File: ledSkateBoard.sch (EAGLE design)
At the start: 24 parts, among them U1 MPU-9150, U2 ATMEGA328P_TQFP, U4 MIC2505 3.3

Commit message: Initial route of board
Still need to add test pads for debugging.
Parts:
- removed D4, D5: (no value), SparkFun-DiscreteSemi:DIODESOD523
- added D2, D3: RB751, SparkFun-DiscreteSemi:DIODE-SCHOTTKY-RB751
- added JP3: LED CONNECTOR, SparkFun-Connectors:M03PTH
- added R6: 4.3K, SparkFun-Resistors:RESISTOR0603-RES
- added R7: 36K, SparkFun-Resistors:RESISTOR0603-RES
- added TP1: TEST-POINT3, SparkFun-Passives:TEST-POINT3
- J1: value (none) -> JST
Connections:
- new net DATA: JP3.2, U2.PB0(ICP)
- new net N$4: R6.1, R7.2, U2.PC0(ADC0)
- net 5V: now also D2.A; no longer D4.A
- net GND: now also JP3.3, R7.1
- net N$3: now also D2.C, D3.C; no longer D4.C, D5.C
- net VCC: now also U2.AREF
- net V_BATT: now also D3.A, JP3.1, R6.2; no longer D5.A
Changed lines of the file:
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@@
 <part name="C5" library="SparkFun-Capacitors" deviceset="CAP" device="PTH" value="4.7uF"/>
 <part name="GND10" library="SparkFun-Aesthetics" deviceset="GND" device=""/>
-<part name="J1" library="SparkFun-Connectors" deviceset="JST_2MM_MALE" device=""/>
+<part name="J1" library="SparkFun-Connectors" deviceset="JST_2MM_MALE" device="" value="JST"/>
 <part name="GND11" library="SparkFun-Aesthetics" deviceset="GND" device=""/>
 <part name="U4" library="SparkFun-PowerIC" deviceset="MIC5205" device="3.3V" value="MIC2505 3.3"/>
@@
 <part name="SUPPLY10" library="SparkFun-Aesthetics" deviceset="5V" device=""/>
 <part name="SUPPLY11" library="SparkFun-Aesthetics" deviceset="5V" device=""/>
-<part name="D4" library="SparkFun-DiscreteSemi" deviceset="DIODE" device="SOD523"/>
-<part name="D5" library="SparkFun-DiscreteSemi" deviceset="DIODE" device="SOD523"/>
+<part name="R6" library="SparkFun-Resistors" deviceset="RESISTOR" device="0603-RES" value="4.3K"/>
+<part name="R7" library="SparkFun-Resistors" deviceset="RESISTOR" device="0603-RES" value="36K"/>
+<part name="GND18" library="SparkFun-Aesthetics" deviceset="GND" device=""/>
+<part name="SUPPLY12" library="SparkFun-Aesthetics" deviceset="V_BATT" device=""/>
+<part name="JP3" library="SparkFun-Connectors" deviceset="M03" device="PTH" value="LED CONNECTOR"/>
+<part name="SUPPLY13" library="SparkFun-Aesthetics" deviceset="V_BATT" device=""/>
+<part name="GND19" library="SparkFun-Aesthetics" deviceset="GND" device=""/>
+<part name="D2" library="SparkFun-DiscreteSemi" deviceset="DIODE-SCHOTTKY" device="-RB751" value="RB751"/>
+<part name="D3" library="SparkFun-DiscreteSemi" deviceset="DIODE-SCHOTTKY" device="-RB751" value="RB751"/>
+<part name="TP1" library="SparkFun-Passives" deviceset="TEST-POINT" device="3"/>
 </parts>
 <sheets>
@@
 <instance part="SUPPLY10" gate="G$1" x="5.08" y="7.62"/>
 <instance part="SUPPLY11" gate="G$1" x="-15.24" y="119.38"/>
-<instance part="D4" gate="G$1" x="-15.24" y="114.3" rot="R270"/>
-<instance part="D5" gate="G$1" x="-7.62" y="114.3" rot="R270"/>
+<instance part="R6" gate="G$1" x="154.94" y="119.38" rot="R90"/>
+<instance part="R7" gate="G$1" x="154.94" y="106.68" rot="R90"/>
+<instance part="GND18" gate="1" x="154.94" y="96.52"/>
+<instance part="SUPPLY12" gate="G$1" x="154.94" y="127"/>
+<instance part="JP3" gate="G$1" x="198.12" y="99.06" rot="R180"/>
+<instance part="SUPPLY13" gate="G$1" x="185.42" y="106.68"/>
+<instance part="GND19" gate="1" x="185.42" y="88.9"/>
+<instance part="D2" gate="G$1" x="-15.24" y="114.3" rot="R270"/>
+<instance part="D3" gate="G$1" x="-7.62" y="114.3" rot="R270"/>
+<instance part="TP1" gate="G$1" x="55.88" y="33.02"/>
 </instances>
 <busses>
@@
 <wire x1="58.42" y1="106.68" x2="58.42" y2="111.76" width="0.1524" layer="91"/>
 <junction x="58.42" y="106.68"/>
+<wire x1="73.66" y1="101.6" x2="73.66" y2="96.52" width="0.1524" layer="91"/>
+<junction x="73.66" y="101.6"/>
+<pinref part="U2" gate="U$1" pin="AREF"/>
+<wire x1="73.66" y1="96.52" x2="83.82" y2="96.52" width="0.1524" layer="91"/>
 </segment>
 <segment>
@@
 <pinref part="GND17" gate="1" pin="GND"/>
 </segment>
+<segment>
+<pinref part="R7" gate="G$1" pin="1"/>
+<wire x1="154.94" y1="101.6" x2="154.94" y2="99.06" width="0.1524" layer="91"/>
+<pinref part="GND18" gate="1" pin="GND"/>
+</segment>
+<segment>
+<pinref part="JP3" gate="G$1" pin="3"/>
+<wire x1="190.5" y1="96.52" x2="185.42" y2="96.52" width="0.1524" layer="91"/>
+<wire x1="185.42" y1="96.52" x2="185.42" y2="91.44" width="0.1524" layer="91"/>
+<pinref part="GND19" gate="1" pin="GND"/>
+</segment>
 </net>
 <net name="V_BATT" class="0">
@@
 </segment>
 <segment>
-<pinref part="D5" gate="G$1" pin="A"/>
 <pinref part="SUPPLY3" gate="G$1" pin="V_BATT"/>
 <wire x1="-7.62" y1="116.84" x2="-7.62" y2="119.38" width="0.1524" layer="91"/>
+<pinref part="D3" gate="G$1" pin="A"/>
+</segment>
+<segment>
+<pinref part="R6" gate="G$1" pin="2"/>
+<wire x1="154.94" y1="124.46" x2="154.94" y2="127" width="0.1524" layer="91"/>
+<pinref part="SUPPLY12" gate="G$1" pin="V_BATT"/>
+</segment>
+<segment>
+<pinref part="JP3" gate="G$1" pin="1"/>
+<wire x1="190.5" y1="101.6" x2="185.42" y2="101.6" width="0.1524" layer="91"/>
+<wire x1="185.42" y1="101.6" x2="185.42" y2="106.68" width="0.1524" layer="91"/>
+<pinref part="SUPPLY13" gate="G$1" pin="V_BATT"/>
 </segment>
 </net>
@@
 </segment>
 <segment>
-<pinref part="D4" gate="G$1" pin="A"/>
 <pinref part="SUPPLY11" gate="G$1" pin="5V"/>
 <wire x1="-15.24" y1="116.84" x2="-15.24" y2="119.38" width="0.1524" layer="91"/>
+<pinref part="D2" gate="G$1" pin="A"/>
 </segment>
 </net>
@@
 <pinref part="U4" gate="G$1" pin="EN"/>
 <wire x1="-7.62" y1="106.68" x2="-15.24" y2="106.68" width="0.1524" layer="91"/>
-<pinref part="D4" gate="G$1" pin="C"/>
 <wire x1="-15.24" y1="111.76" x2="-15.24" y2="106.68" width="0.1524" layer="91"/>
-<pinref part="D5" gate="G$1" pin="C"/>
 <wire x1="-7.62" y1="111.76" x2="-7.62" y2="106.68" width="0.1524" layer="91"/>
-</segment>
-</net>
+<pinref part="D2" gate="G$1" pin="C"/>
+<pinref part="D3" gate="G$1" pin="C"/>
+</segment>
+</net>
+<net name="N$4" class="0">
+<segment>
+<pinref part="U2" gate="U$1" pin="PC0(ADC0)"/>
+<pinref part="R7" gate="G$1" pin="2"/>
+<wire x1="132.08" y1="111.76" x2="154.94" y2="111.76" width="0.1524" layer="91"/>
+<pinref part="R6" gate="G$1" pin="1"/>
+<wire x1="154.94" y1="114.3" x2="154.94" y2="111.76" width="0.1524" layer="91"/>
+<junction x="154.94" y="111.76"/>
+</segment>
+</net>
+<net name="DATA" class="0">
+<segment>
+<pinref part="U2" gate="U$1" pin="PB0(ICP)"/>
+<wire x1="132.08" y1="66.04" x2="139.7" y2="66.04" width="0.1524" layer="91"/>
+<label x="134.62" y="66.04" size="1.778" layer="95"/>
+</segment>
+<segment>
+<pinref part="JP3" gate="G$1" pin="2"/>
+<wire x1="190.5" y1="99.06" x2="185.42" y2="99.06" width="0.1524" layer="91"/>
+<label x="182.88" y="99.06" size="1.778" layer="95"/>
+</segment>
+</net>

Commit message: Final version before ordering.
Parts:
- removed C2, C3: 10uF, SparkFun-Capacitors:CAPPTH
- removed C4, C5, C6, C7: 4.7uF, SparkFun-Capacitors:CAPPTH
- removed C8: .1uF, SparkFun-Capacitors:CAPPTH
- removed R1, R2: 10K, SparkFun-Resistors:RESISTOR0603-RES
- removed R3: 330, SparkFun-Resistors:RESISTOR0603-RES
- removed R4: 2K, SparkFun-Resistors:RESISTOR0603-RES
- removed R5: 1K, SparkFun-Resistors:RESISTOR0603-RES
- removed R6: 4.3K, SparkFun-Resistors:RESISTOR0603-RES
- removed R7: 36K, SparkFun-Resistors:RESISTOR0603-RES
- removed TP1: TEST-POINT3, SparkFun-Passives:TEST-POINT3
- added C10, C11, C12, C9: 4.7uF, SparkFun-Capacitors:CAP0805
- added C13: .1uF, SparkFun-Capacitors:CAP0805
- added C14, C15, C17: 10uF, SparkFun-Capacitors:CAP0805
- added R10: 36K, SparkFun-Resistors:RESISTOR0805-RES
- added R11, R12: 10K, SparkFun-Resistors:RESISTOR0805-RES
- added R13: 330, SparkFun-Resistors:RESISTOR0805-RES
- added R14: 2K, SparkFun-Resistors:RESISTOR0805-RES
- added R8: 1K, SparkFun-Resistors:RESISTOR0805-RES
- added R9: 4.3K, SparkFun-Resistors:RESISTOR0805-RES
- added TP3: TEST-POINT3, SparkFun-Passives:TEST-POINT3
- C1: device SparkFun-Capacitors:CAPPTH -> SparkFun-Capacitors:CAP0805
- D2, D3: value RB751 -> Schottky .35Vf; device SparkFun-DiscreteSemi:DIODE-SCHOTTKY-RB751 -> microbuilder:DIODESMA
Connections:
- net 5V: now also C9.1, R13.2; no longer C4.1, R3.2
- net GND: now also C1.1, C10.2, C11.2, C12.2, C13.1, C14.1, C15.1, C17.1, C9.2, R10.1, R14.1; no longer C1.2, C2.2, C3.2, C4.2, C5.2, C6.2, C7.2, C8.1, R4.1, R7.1
- net N$1: now also C11.1; no longer C6.1
- net N$11: now also R14.2; no longer R4.2
- net N$2: now also C12.1; no longer C7.1
- net N$3: now also C14.2; no longer C1.1
- net N$4: now also R10.2, R9.1, TP3.1; no longer R6.1, R7.2
- net N$7: now also R13.1; no longer R3.1
- net RESET: now also R8.1; no longer R5.1
- net SCL: now also R12.1; no longer R2.1
- net SDA: now also R11.1; no longer R1.1
- net VCC: now also C1.2, C13.2, C15.2, C17.2, R11.2, R12.2, R8.2; no longer C2.1, C3.1, C8.2, R1.2, R2.2, R5.2
- net V_BATT: now also C10.1, R9.2; no longer C5.1, R6.2
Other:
- moved on the sheet: C1

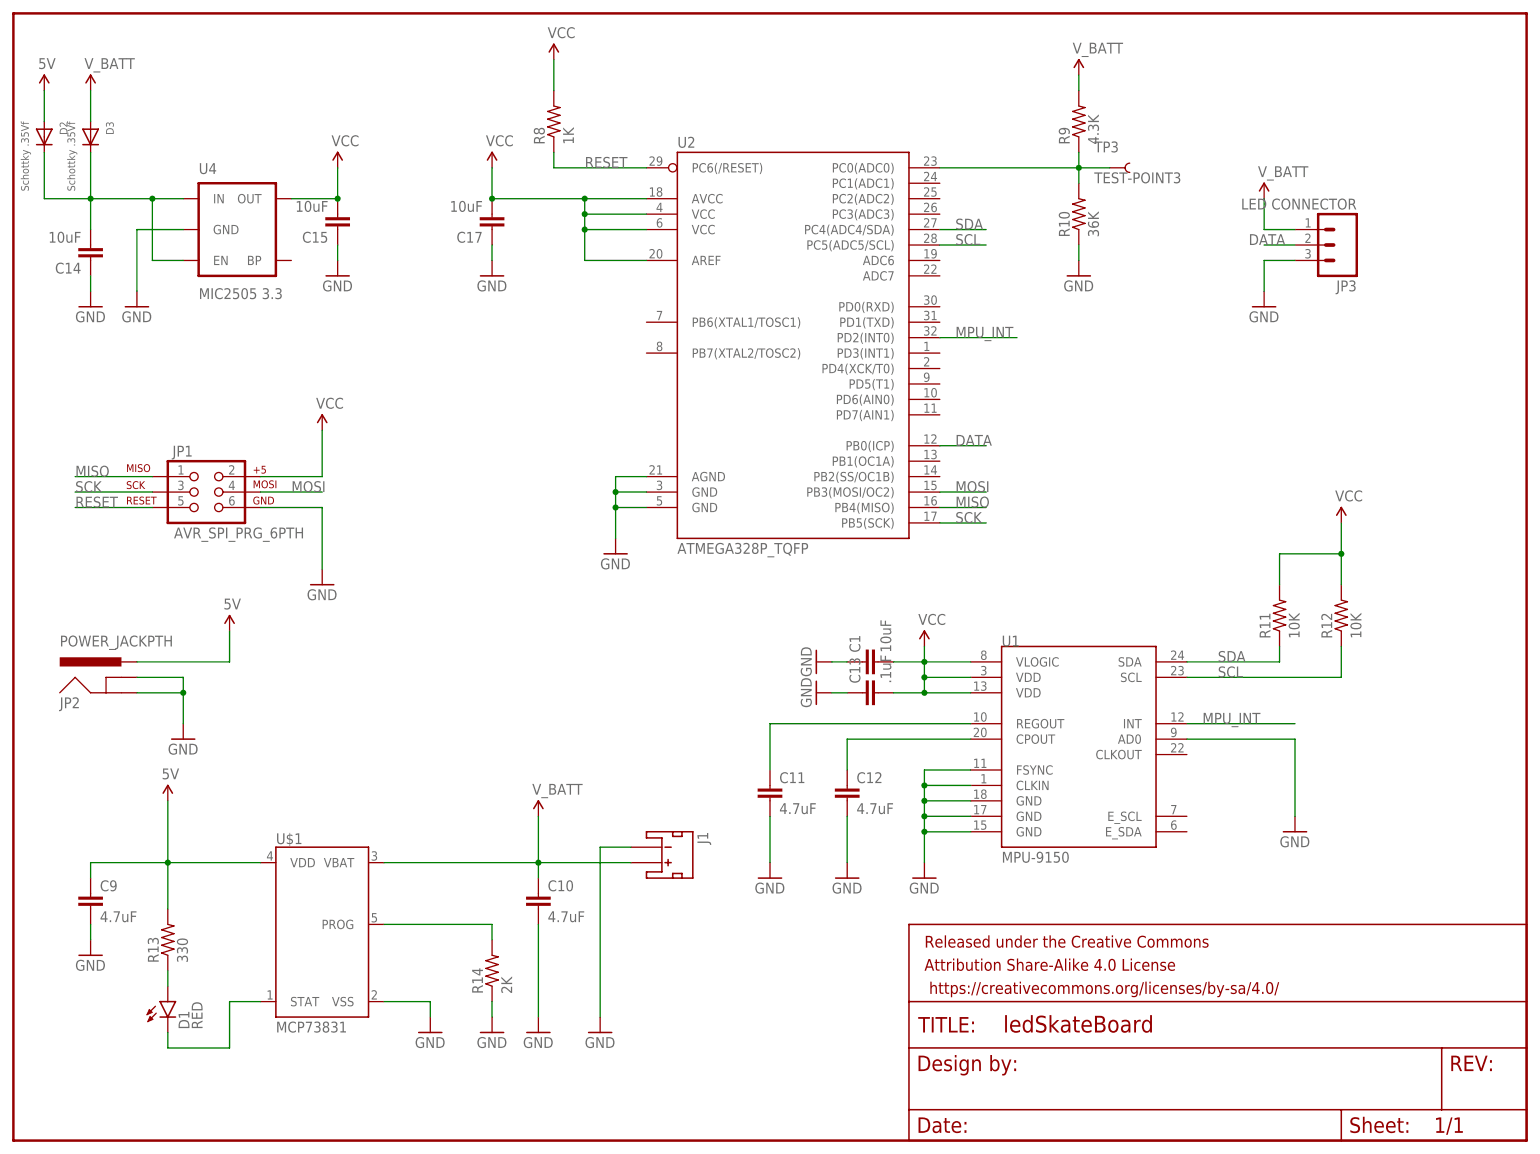
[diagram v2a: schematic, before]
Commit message: Learned how to use Smash tool. Redid silkscreen
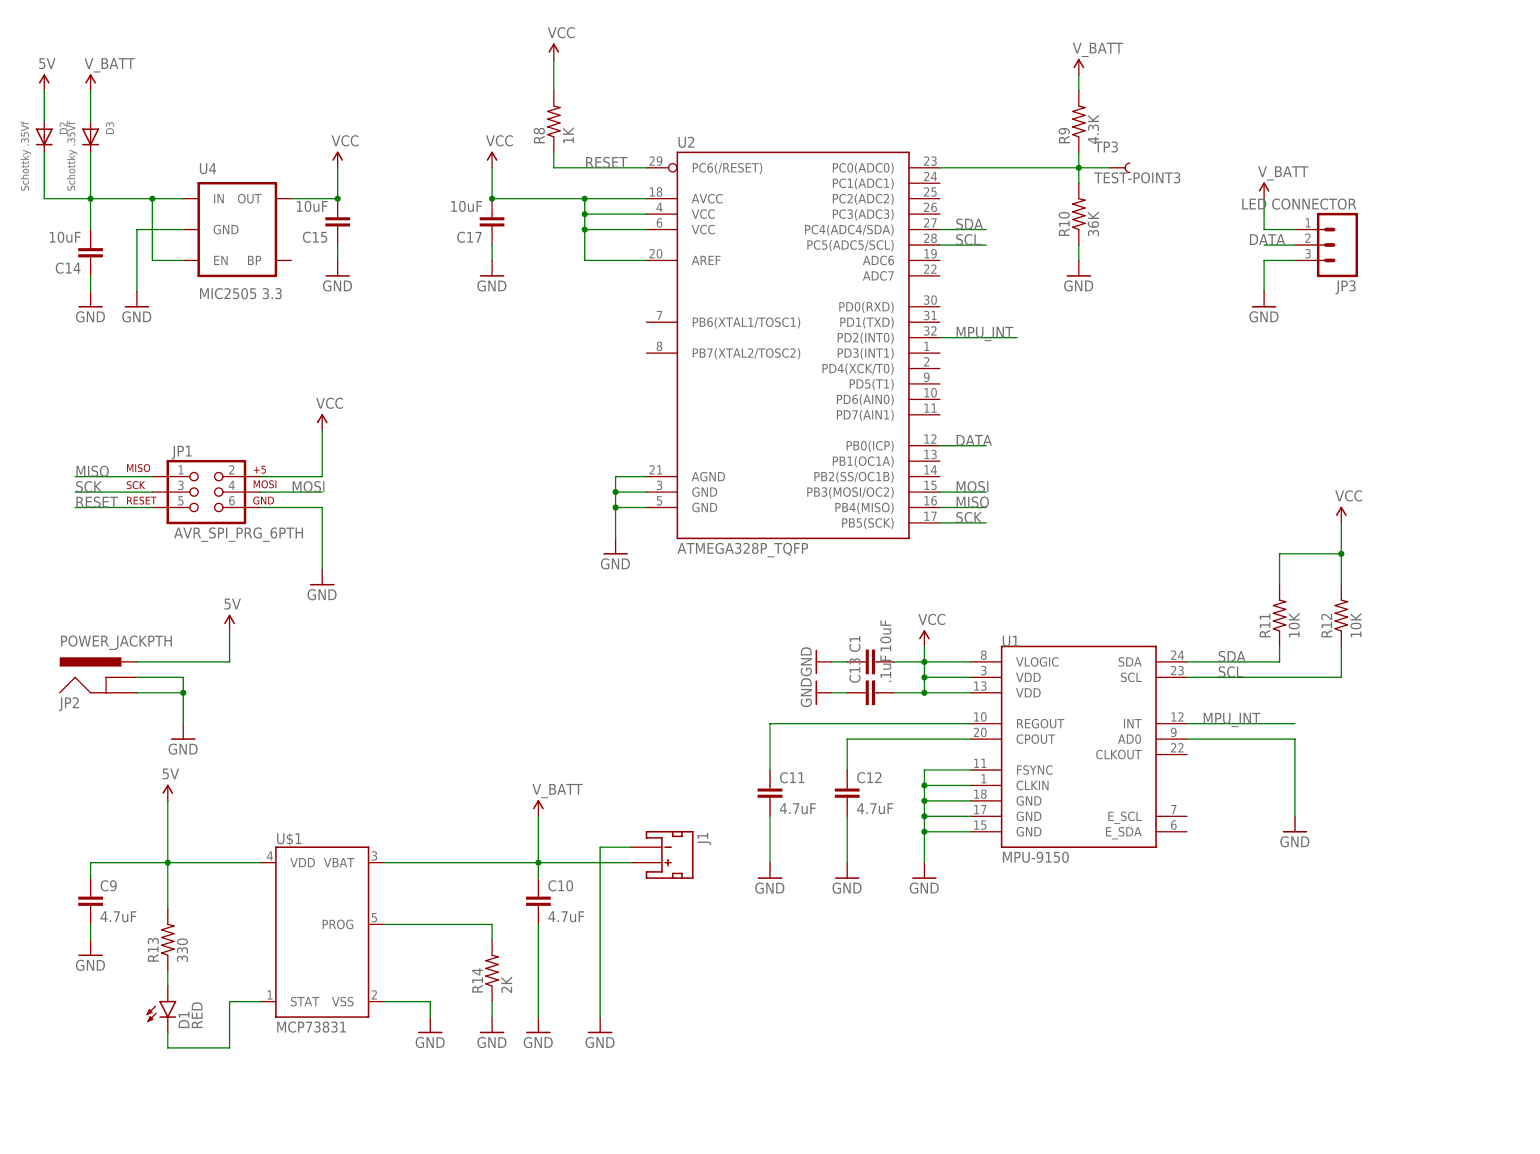
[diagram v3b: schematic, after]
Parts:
- removed FRAME1: (no value), SparkFun-Aesthetics:FRAME-LETTER
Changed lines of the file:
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@@
 </classes>
 <parts>
-<part name="FRAME1" library="SparkFun-Aesthetics" deviceset="FRAME-LETTER" device=""/>
 <part name="JP1" library="SparkFun-Connectors" deviceset="AVR_SPI_PRG_6" device="PTH"/>
 <part name="U2" library="SparkFun-DigitalIC" deviceset="ATMEGA328P_TQFP" device="" value="ATMEGA328P_TQFP"/>
@@
 </plain>
 <instances>
-<instance part="FRAME1" gate="G$1" x="-20.32" y="-48.26"/>
-<instance part="FRAME1" gate="V" x="127" y="-48.26"/>
 <instance part="JP1" gate="G$1" x="10.16" y="58.42"/>
 <instance part="U2" gate="U$1" x="109.22" y="81.28"/>

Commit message: First commit
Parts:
- removed D2, D3: Schottky .35Vf, microbuilder:DIODESMA
- removed JP2: POWER_JACKPTH, SparkFun-Connectors:POWER_JACKPTH
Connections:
- removed net N$3: C14.2, D2.C, D3.C, U4.EN, U4.IN
- net 5V: no longer D2.A, JP2.PWR
- net GND: no longer JP2.GND, JP2.GNDBREAK
- net V_BATT: now also C14.2, U4.EN, U4.IN; no longer D3.A
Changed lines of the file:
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@@
 <part name="GND16" library="SparkFun-Aesthetics" deviceset="GND" device=""/>
 <part name="SUPPLY9" library="SparkFun-Aesthetics" deviceset="VCC" device=""/>
-<part name="JP2" library="SparkFun-Connectors" deviceset="POWER_JACK" device="PTH"/>
-<part name="GND17" library="SparkFun-Aesthetics" deviceset="GND" device=""/>
-<part name="SUPPLY5" library="SparkFun-Aesthetics" deviceset="5V" device=""/>
 <part name="SUPPLY10" library="SparkFun-Aesthetics" deviceset="5V" device=""/>
-<part name="SUPPLY11" library="SparkFun-Aesthetics" deviceset="5V" device=""/>
 <part name="GND18" library="SparkFun-Aesthetics" deviceset="GND" device=""/>
 <part name="SUPPLY12" library="SparkFun-Aesthetics" deviceset="V_BATT" device=""/>
@@
 <part name="GND19" library="SparkFun-Aesthetics" deviceset="GND" device=""/>
 <part name="TP3" library="SparkFun-Passives" deviceset="TEST-POINT" device="3"/>
-<part name="D2" library="microbuilder" deviceset="DIODE" device="SMA" value="Schottky .35Vf"/>
-<part name="D3" library="microbuilder" deviceset="DIODE" device="SMA" value="Schottky .35Vf"/>
 <part name="R8" library="SparkFun-Resistors" deviceset="RESISTOR" device="0805-RES" value="1K"/>
 <part name="R9" library="SparkFun-Resistors" deviceset="RESISTOR" device="0805-RES" value="4.3K"/>
@@
 <instance part="GND16" gate="1" x="111.76" y="25.4" rot="R270"/>
 <instance part="SUPPLY9" gate="G$1" x="68.58" y="129.54"/>
-<instance part="JP2" gate="G$1" x="-2.54" y="22.86"/>
-<instance part="GND17" gate="1" x="7.62" y="17.78"/>
-<instance part="SUPPLY5" gate="G$1" x="15.24" y="35.56"/>
 <instance part="SUPPLY10" gate="G$1" x="5.08" y="7.62"/>
-<instance part="SUPPLY11" gate="G$1" x="-15.24" y="124.46"/>
 <instance part="GND18" gate="1" x="154.94" y="93.98"/>
 <instance part="SUPPLY12" gate="G$1" x="154.94" y="127"/>
@@
 <instance part="GND19" gate="1" x="185.42" y="88.9"/>
 <instance part="TP3" gate="G$1" x="160.02" y="111.76"/>
-<instance part="D2" gate="G$1" x="-15.24" y="116.84" rot="R270"/>
-<instance part="D3" gate="G$1" x="-7.62" y="116.84" rot="R270"/>
 <instance part="R8" gate="G$1" x="68.58" y="119.38" rot="R90"/>
 <instance part="R9" gate="G$1" x="154.94" y="119.38" rot="R90"/>
@@
 </segment>
 <segment>
-<pinref part="JP2" gate="G$1" pin="GNDBREAK"/>
-<wire x1="0" y1="27.94" x2="7.62" y2="27.94" width="0.1524" layer="91"/>
-<wire x1="7.62" y1="27.94" x2="7.62" y2="25.4" width="0.1524" layer="91"/>
-<pinref part="JP2" gate="G$1" pin="GND"/>
-<wire x1="0" y1="25.4" x2="7.62" y2="25.4" width="0.1524" layer="91"/>
-<wire x1="7.62" y1="25.4" x2="7.62" y2="20.32" width="0.1524" layer="91"/>
-<junction x="7.62" y="25.4"/>
-<pinref part="GND17" gate="1" pin="GND"/>
-</segment>
-<segment>
 <pinref part="JP3" gate="G$1" pin="3"/>
 <wire x1="190.5" y1="96.52" x2="185.42" y2="96.52" width="0.1524" layer="91"/>
@@
 </segment>
 <segment>
-<pinref part="D3" gate="G$1" pin="A"/>
 <pinref part="SUPPLY3" gate="G$1" pin="V_BATT"/>
-<wire x1="-7.62" y1="119.38" x2="-7.62" y2="124.46" width="0.1524" layer="91"/>
+<wire x1="7.62" y1="106.68" x2="2.54" y2="106.68" width="0.1524" layer="91"/>
+<wire x1="2.54" y1="106.68" x2="-7.62" y2="106.68" width="0.1524" layer="91"/>
+<wire x1="7.62" y1="96.52" x2="2.54" y2="96.52" width="0.1524" layer="91"/>
+<wire x1="2.54" y1="96.52" x2="2.54" y2="106.68" width="0.1524" layer="91"/>
+<junction x="2.54" y="106.68"/>
+<junction x="-7.62" y="106.68"/>
+<pinref part="U4" gate="G$1" pin="IN"/>
+<pinref part="U4" gate="G$1" pin="EN"/>
+<wire x1="-7.62" y1="124.46" x2="-7.62" y2="106.68" width="0.1524" layer="91"/>
+<pinref part="C14" gate="G$1" pin="2"/>
+<wire x1="-7.62" y1="101.6" x2="-7.62" y2="106.68" width="0.1524" layer="91"/>
 </segment>
 <segment>
@@
 </net>
 <net name="5V" class="0">
-<segment>
-<pinref part="JP2" gate="G$1" pin="PWR"/>
-<wire x1="0" y1="30.48" x2="15.24" y2="30.48" width="0.1524" layer="91"/>
-<wire x1="15.24" y1="30.48" x2="15.24" y2="35.56" width="0.1524" layer="91"/>
-<pinref part="SUPPLY5" gate="G$1" pin="5V"/>
-</segment>
 <segment>
 <pinref part="U$1" gate="G$1" pin="VDD"/>
@@
 <pinref part="C9" gate="G$1" pin="1"/>
 </segment>
-<segment>
-<pinref part="D2" gate="G$1" pin="A"/>
-<pinref part="SUPPLY11" gate="G$1" pin="5V"/>
-<wire x1="-15.24" y1="119.38" x2="-15.24" y2="124.46" width="0.1524" layer="91"/>
-</segment>
-</net>
-<net name="N$3" class="0">
-<segment>
-<wire x1="7.62" y1="106.68" x2="2.54" y2="106.68" width="0.1524" layer="91"/>
-<wire x1="2.54" y1="106.68" x2="-7.62" y2="106.68" width="0.1524" layer="91"/>
-<wire x1="7.62" y1="96.52" x2="2.54" y2="96.52" width="0.1524" layer="91"/>
-<wire x1="2.54" y1="96.52" x2="2.54" y2="106.68" width="0.1524" layer="91"/>
-<junction x="2.54" y="106.68"/>
-<junction x="-7.62" y="106.68"/>
-<pinref part="U4" gate="G$1" pin="IN"/>
-<pinref part="U4" gate="G$1" pin="EN"/>
-<wire x1="-7.62" y1="106.68" x2="-15.24" y2="106.68" width="0.1524" layer="91"/>
-<wire x1="-15.24" y1="114.3" x2="-15.24" y2="106.68" width="0.1524" layer="91"/>
-<wire x1="-7.62" y1="114.3" x2="-7.62" y2="106.68" width="0.1524" layer="91"/>
-<pinref part="D2" gate="G$1" pin="C"/>
-<pinref part="D3" gate="G$1" pin="C"/>
-<pinref part="C14" gate="G$1" pin="2"/>
-<wire x1="-7.62" y1="101.6" x2="-7.62" y2="106.68" width="0.1524" layer="91"/>
-</segment>
-</net>
+</net>
